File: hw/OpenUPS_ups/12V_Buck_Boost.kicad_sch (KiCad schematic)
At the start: 61 parts, among them Q601 AON7534, Q602 AON7534, Q603 AON7534, Q604 AON7534, U601 NCP81599

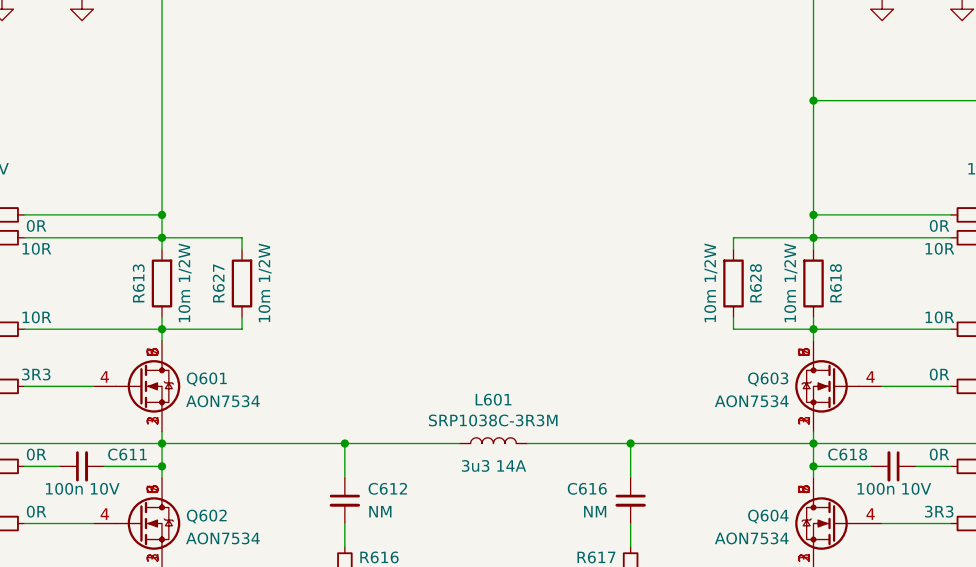
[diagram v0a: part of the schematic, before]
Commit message: 12V converter layout
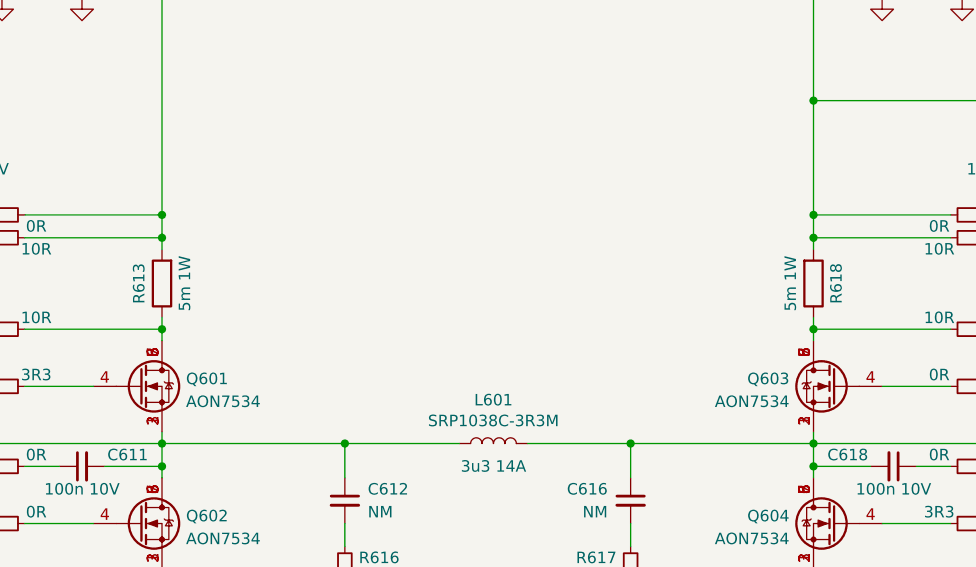
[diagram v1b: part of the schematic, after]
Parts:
- removed R627, R628: 10m 1/2W, Resistor_SMD:R_1206_3216Metric, symbol Device:R
- R613, R618: value 10m 1/2W -> 5m 1W
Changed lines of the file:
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@@
-    (stroke (width 0) (type default))
-  )
-  (wire (pts (xy 116.84 73.66) (xy 107.95 73.66))
     (stroke (width 0) (type default))
   )
@@
     (stroke (width 0) (type default))
   )
-  (wire (pts (xy 116.84 63.5) (xy 107.95 63.5))
-    (stroke (width 0) (type default))
-  )
   (wire (pts (xy 154.94 139.7) (xy 156.21 139.7))
     (stroke (width 0) (type default))
@@
     (stroke (width 0) (type default))
   )
-  (wire (pts (xy 116.84 64.77) (xy 116.84 63.5))
-    (stroke (width 0) (type default))
-  )
   (wire (pts (xy 237.49 63.5) (xy 237.49 66.04))
     (stroke (width 0) (type default))
@@
     (stroke (width 0) (type default))
   )
-  (wire (pts (xy 171.45 72.39) (xy 171.45 73.66))
-    (stroke (width 0) (type default))
-  )
   (wire (pts (xy 72.39 95.25) (xy 87.63 95.25))
     (stroke (width 0) (type default))
   )
-  (wire (pts (xy 171.45 64.77) (xy 171.45 63.5))
-    (stroke (width 0) (type default))
-  )
   (wire (pts (xy 107.95 88.9) (xy 107.95 90.17))
     (stroke (width 0) (type default))
@@
     (stroke (width 0) (type default))
   )
-  (wire (pts (xy 171.45 63.5) (xy 180.34 63.5))
-    (stroke (width 0) (type default))
-  )
   (wire (pts (xy 90.17 162.56) (xy 115.57 162.56))
     (stroke (width 0) (type default))
@@
     (stroke (width 0) (type default))
   )
-  (wire (pts (xy 116.84 72.39) (xy 116.84 73.66))
-    (stroke (width 0) (type default))
-  )
   (wire (pts (xy 208.28 63.5) (xy 200.66 63.5))
     (stroke (width 0) (type default))
   )
   (wire (pts (xy 170.18 149.86) (xy 172.72 149.86))
-    (stroke (width 0) (type default))
-  )
-  (wire (pts (xy 171.45 73.66) (xy 180.34 73.66))
     (stroke (width 0) (type default))
   )
@@
       (effects (font (size 1.27 1.27)))
     )
-    (property "Value" "10m 1/2W" (at 110.49 68.58 90)
+    (property "Value" "5m 1W" (at 110.49 68.58 90)
       (effects (font (size 1.27 1.27)))
     )
@@
     )
   )
-  (symbol (lib_id "Device:R") (at 171.45 68.58 0) (mirror x) (unit 1)
-    (in_bom yes) (on_board yes) (dnp no)
-    (property "Reference" "R628" (at 173.99 68.58 90)
-      (effects (font (size 1.27 1.27)))
-    )
-    (property "Value" "10m 1/2W" (at 168.91 68.58 90)
-      (effects (font (size 1.27 1.27)))
-    )
-    (property "Footprint" "Resistor_SMD:R_1206_3216Metric" (at 169.672 68.58 90)
-      (effects (font (size 1.27 1.27)) hide)
-    )
-    (property "Datasheet" "~" (at 171.45 68.58 0)
-      (effects (font (size 1.27 1.27)) hide)
-    )
-    (pin "1")
-    (pin "2")
-    (instances
-      (project "OpenUPS_ups"
-        (path "/f77faec3-eac4-47f3-a2de-ec4a039f4502/09fcd86a-cc7e-4bce-97cb-42a94055ba63"
-          (reference "R628") (unit 1)
-        )
-        (path "/f77faec3-eac4-47f3-a2de-ec4a039f4502/dfbaaed0-e564-4e21-900d-d5a65c0f1694"
-          (reference "R328") (unit 1)
-        )
-        (path "/f77faec3-eac4-47f3-a2de-ec4a039f4502/0bd99307-a15c-41e8-997b-077d576f806c"
-          (reference "R417") (unit 1)
-        )
-      )
-    )
-  )
   (symbol (lib_id "Device:C_Small") (at 160.02 92.71 0) (mirror y) (unit 1)
     (in_bom yes) (on_board yes) (dnp no)
@@
         (path "/f77faec3-eac4-47f3-a2de-ec4a039f4502/dfbaaed0-e564-4e21-900d-d5a65c0f1694"
           (reference "#PWR0316") (unit 1)
-        )
-      )
-    )
-  )
-  (symbol (lib_id "Device:R") (at 116.84 68.58 180) (unit 1)
-    (in_bom yes) (on_board yes) (dnp no)
-    (property "Reference" "R627" (at 114.3 68.58 90)
-      (effects (font (size 1.27 1.27)))
-    )
-    (property "Value" "10m 1/2W" (at 119.38 68.58 90)
-      (effects (font (size 1.27 1.27)))
-    )
-    (property "Footprint" "Resistor_SMD:R_1206_3216Metric" (at 118.618 68.58 90)
-      (effects (font (size 1.27 1.27)) hide)
-    )
-    (property "Datasheet" "~" (at 116.84 68.58 0)
-      (effects (font (size 1.27 1.27)) hide)
-    )
-    (pin "1")
-    (pin "2")
-    (instances
-      (project "OpenUPS_ups"
-        (path "/f77faec3-eac4-47f3-a2de-ec4a039f4502/09fcd86a-cc7e-4bce-97cb-42a94055ba63"
-          (reference "R627") (unit 1)
-        )
-        (path "/f77faec3-eac4-47f3-a2de-ec4a039f4502/dfbaaed0-e564-4e21-900d-d5a65c0f1694"
-          (reference "R327") (unit 1)
-        )
-        (path "/f77faec3-eac4-47f3-a2de-ec4a039f4502/0bd99307-a15c-41e8-997b-077d576f806c"
-          (reference "R417") (unit 1)
         )
       )
@@
       (effects (font (size 1.27 1.27)))
     )
-    (property "Value" "10m 1/2W" (at 177.8 68.58 90)
-      (effects (font (size 1.27 1.27)))
-    )
+    (property "Value" "5m 1W" (at 177.8 68.58 90)
+      (effects (font (size 1.27 1.27)))
+    )
